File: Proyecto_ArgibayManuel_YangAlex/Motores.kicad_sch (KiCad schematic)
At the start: 10 parts, among them K1 RT314012, K2 RT314012, Q1 2N2222, Q2 2N2222, U2 DRV8871DDA, U3 DRV8871DDA

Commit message: Ordenar esquematico
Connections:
- no-connect marks 2 -> 4
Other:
- moved on the sheet: D1, D2, K1, K2, Q1, Q2, R1, R2, U2, U3

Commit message: footprint
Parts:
- R8: renamed from R2; footprint (none) -> Resistor_THT:R_Axial_DIN0204_L3.6mm_D1.6mm_P1.90mm_Vertical
- R9: renamed from R1; footprint (none) -> Resistor_THT:R_Axial_DIN0204_L3.6mm_D1.6mm_P1.90mm_Vertical
- renumbered U2 to U4, U3 to U5
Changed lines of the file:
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@@
 		(on_board yes)
 		(dnp no)
-		(property "Reference" "#PWR034"
+		(property "Reference" "#PWR017"
 			(at 153.67 96.52 0)
 			(effects
@@
 			(project "Proyecto_ArgibayManuel_YangAlex"
 				(path "/b2dde924-33f5-41ab-a1bf-811873450a89/4b87e8bb-9014-4438-949a-51563e216ea6"
-					(reference "#PWR034")
+					(reference "#PWR017")
 					(unit 1)
 				)
@@
 		(dnp no)
 		(fields_autoplaced yes)
-		(property "Reference" "R2"
+		(property "Reference" "R8"
 			(at 44.45 49.53 90)
 			(effects
@@
 			)
 		)
-		(property "Footprint" ""
+		(property "Footprint" "Resistor_THT:R_Axial_DIN0204_L3.6mm_D1.6mm_P1.90mm_Vertical"
 			(at 44.45 57.658 90)
 			(effects
@@
 			(project "Proyecto_ArgibayManuel_YangAlex"
 				(path "/b2dde924-33f5-41ab-a1bf-811873450a89/4b87e8bb-9014-4438-949a-51563e216ea6"
-					(reference "R2")
+					(reference "R8")
 					(unit 1)
 				)
@@
 		(on_board yes)
 		(dnp no)
-		(property "Reference" "#PWR036"
+		(property "Reference" "#PWR015"
 			(at 54.61 96.52 0)
 			(effects
@@
 			(project "Proyecto_ArgibayManuel_YangAlex"
 				(path "/b2dde924-33f5-41ab-a1bf-811873450a89/4b87e8bb-9014-4438-949a-51563e216ea6"
-					(reference "#PWR036")
+					(reference "#PWR015")
 					(unit 1)
 				)
@@
 		(on_board yes)
 		(dnp no)
-		(property "Reference" "#PWR033"
+		(property "Reference" "#PWR016"
 			(at 152.4 66.04 0)
 			(effects
@@
 			(project "Proyecto_ArgibayManuel_YangAlex"
 				(path "/b2dde924-33f5-41ab-a1bf-811873450a89/4b87e8bb-9014-4438-949a-51563e216ea6"
-					(reference "#PWR033")
+					(reference "#PWR016")
 					(unit 1)
 				)
@@
 		(on_board yes)
 		(dnp no)
-		(property "Reference" "#PWR035"
+		(property "Reference" "#PWR014"
 			(at 40.64 69.85 0)
 			(effects
@@
 			(project "Proyecto_ArgibayManuel_YangAlex"
 				(path "/b2dde924-33f5-41ab-a1bf-811873450a89/4b87e8bb-9014-4438-949a-51563e216ea6"
-					(reference "#PWR035")
+					(reference "#PWR014")
 					(unit 1)
 				)
@@
 		(on_board yes)
 		(dnp no)
-		(property "Reference" "U2"
+		(property "Reference" "U4"
 			(at 151.13 51.562 0)
 			(effects
@@
 			(project "Proyecto_ArgibayManuel_YangAlex"
 				(path "/b2dde924-33f5-41ab-a1bf-811873450a89/4b87e8bb-9014-4438-949a-51563e216ea6"
-					(reference "U2")
+					(reference "U4")
 					(unit 1)
 				)
@@
 		(dnp no)
 		(fields_autoplaced yes)
-		(property "Reference" "R1"
+		(property "Reference" "R9"
 			(at 58.42 77.47 90)
 			(effects
@@
 			)
 		)
-		(property "Footprint" ""
+		(property "Footprint" "Resistor_THT:R_Axial_DIN0204_L3.6mm_D1.6mm_P1.90mm_Vertical"
 			(at 58.42 85.598 90)
 			(effects
@@
 			(project "Proyecto_ArgibayManuel_YangAlex"
 				(path "/b2dde924-33f5-41ab-a1bf-811873450a89/4b87e8bb-9014-4438-949a-51563e216ea6"
-					(reference "R1")
+					(reference "R9")
 					(unit 1)
 				)
@@
 		(on_board yes)
 		(dnp no)
-		(property "Reference" "U3"
+		(property "Reference" "U5"
 			(at 152.146 82.296 0)
 			(effects
@@
 			(project "Proyecto_ArgibayManuel_YangAlex"
 				(path "/b2dde924-33f5-41ab-a1bf-811873450a89/4b87e8bb-9014-4438-949a-51563e216ea6"
-					(reference "U3")
+					(reference "U5")
 					(unit 1)
 				)

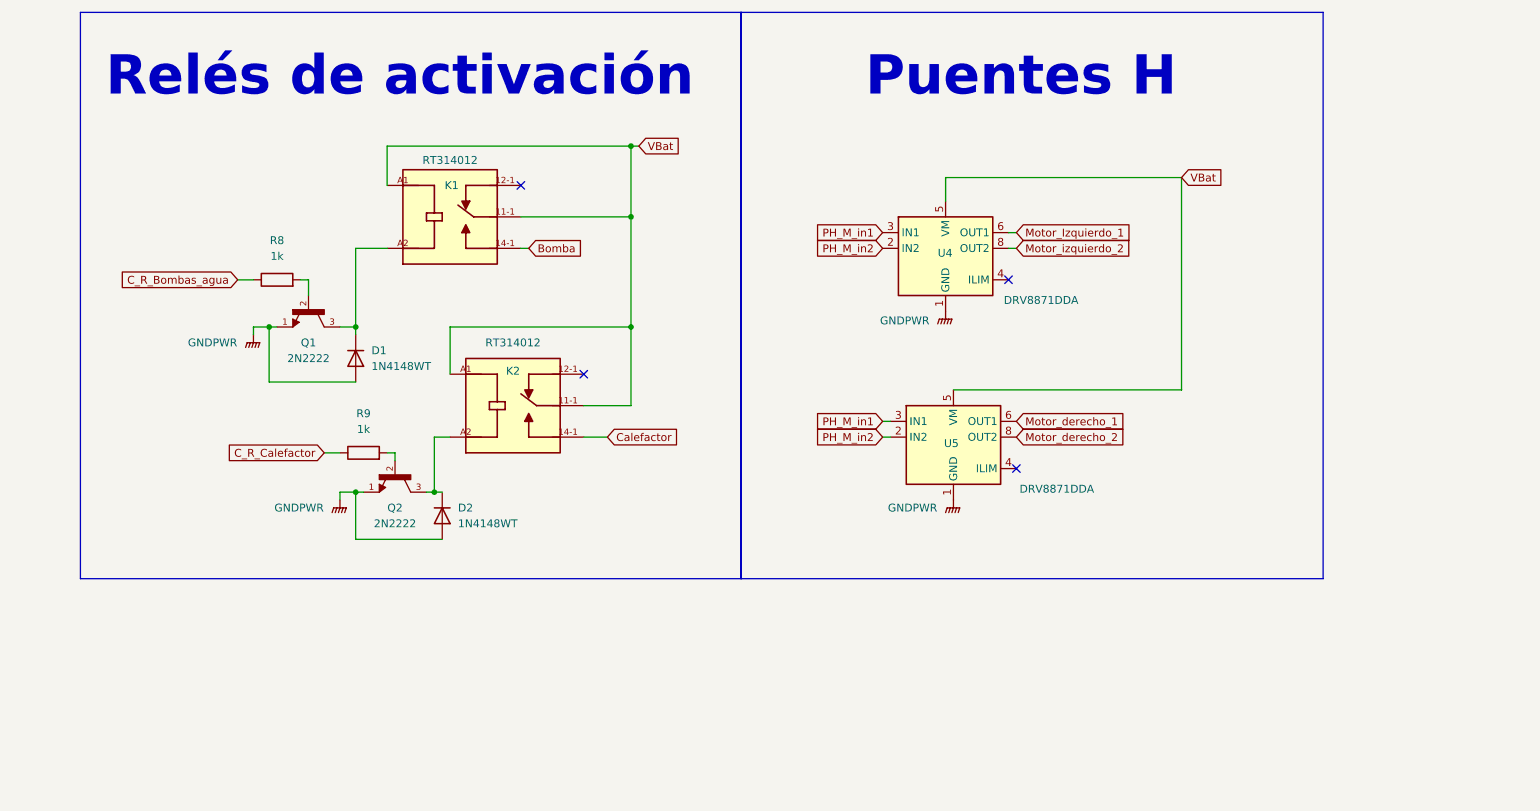
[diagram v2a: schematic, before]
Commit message: Arreglo net classes, agrego DB-9
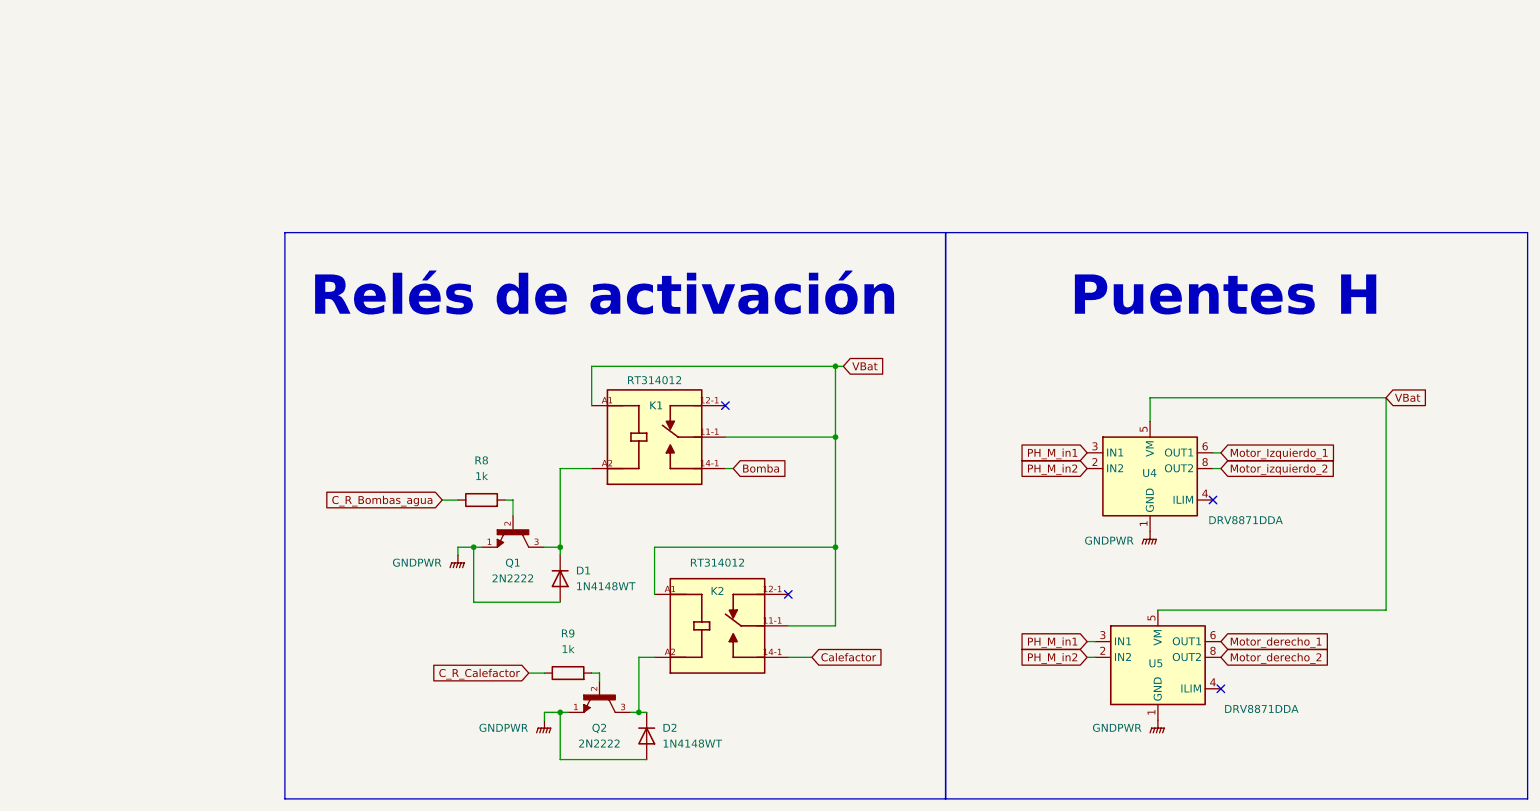
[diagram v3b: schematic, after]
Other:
- company: (none) -> Universidad de Barcelona
- title: (none) -> Circuitos de Potencia
- moved on the sheet: D1, D2, K1, K2, Q1, Q2, R8, R9, U4, U5

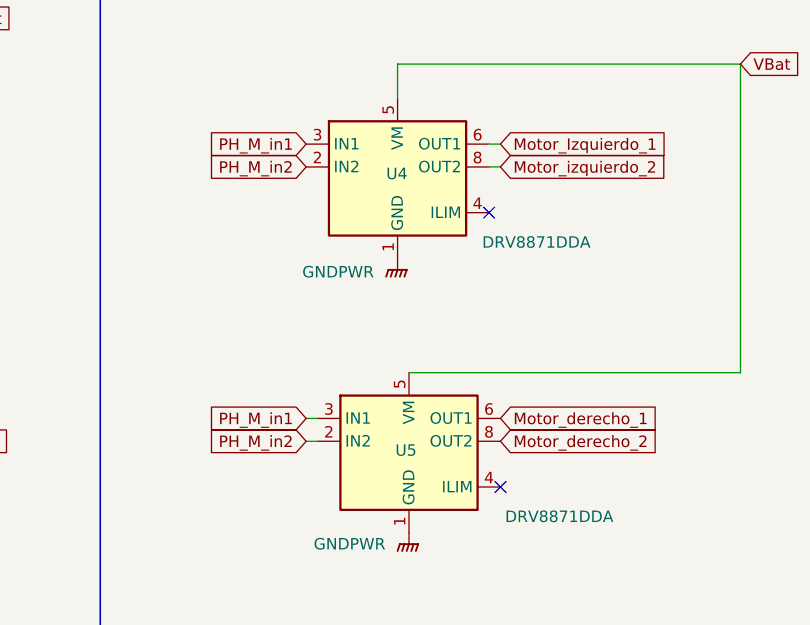
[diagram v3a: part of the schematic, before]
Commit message: Empiezo layout, cambio footprints y arreglo esquematico
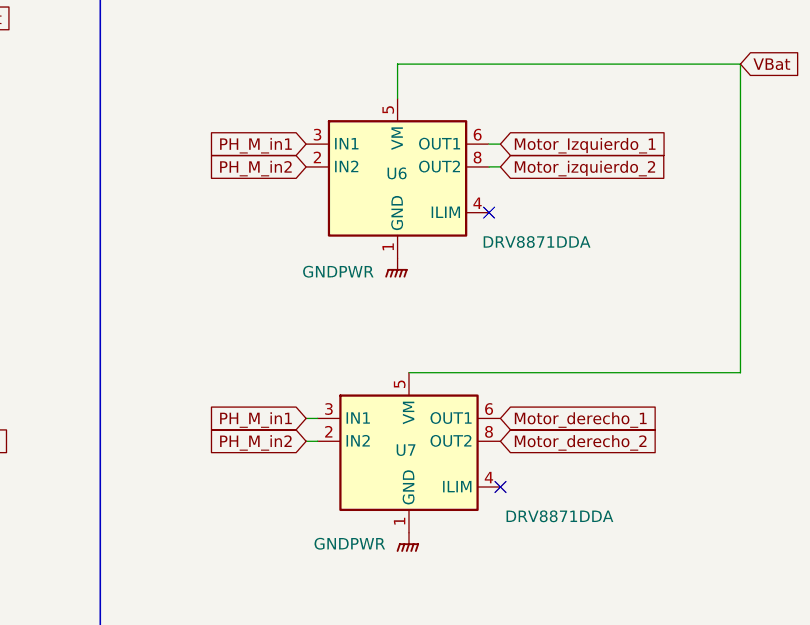
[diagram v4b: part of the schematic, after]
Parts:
- K1, K2: footprint RT314012:RELAY_9-1393239-5 -> Footprints:RT314012
- Q1, Q2: footprint 2N2222:TO127P580H530-3 -> Footprints:2N2222
- R8, R9: footprint Resistor_THT:R_Axial_DIN0204_L3.6mm_D1.6mm_P1.90mm_Vertical -> Resistor_SMD:R_0805_2012Metric
- renumbered U4 to U6, U5 to U7
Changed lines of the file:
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@@
 			)
 		)
-		(property "Footprint" "RT314012:RELAY_9-1393239-5"
+		(property "Footprint" "Footprints:RT314012"
 			(at 115.57 111.76 0)
 			(effects
@@
 		(on_board yes)
 		(dnp no)
-		(property "Reference" "#PWR017"
+		(property "Reference" "#PWR023"
 			(at 186.69 132.08 0)
 			(effects
@@
 			(project "Proyecto_ArgibayManuel_YangAlex"
 				(path "/b2dde924-33f5-41ab-a1bf-811873450a89/4b87e8bb-9014-4438-949a-51563e216ea6"
-					(reference "#PWR017")
+					(reference "#PWR023")
 					(unit 1)
 				)
@@
 			)
 		)
-		(property "Footprint" "Resistor_THT:R_Axial_DIN0204_L3.6mm_D1.6mm_P1.90mm_Vertical"
+		(property "Footprint" "Resistor_SMD:R_0805_2012Metric"
 			(at 77.47 93.218 90)
 			(effects
@@
 		(on_board yes)
 		(dnp no)
-		(property "Reference" "#PWR015"
+		(property "Reference" "#PWR021"
 			(at 87.63 132.08 0)
 			(effects
@@
 			(project "Proyecto_ArgibayManuel_YangAlex"
 				(path "/b2dde924-33f5-41ab-a1bf-811873450a89/4b87e8bb-9014-4438-949a-51563e216ea6"
-					(reference "#PWR015")
+					(reference "#PWR021")
 					(unit 1)
 				)
@@
 		(on_board yes)
 		(dnp no)
-		(property "Reference" "#PWR016"
+		(property "Reference" "#PWR022"
 			(at 185.42 101.6 0)
 			(effects
@@
 			(project "Proyecto_ArgibayManuel_YangAlex"
 				(path "/b2dde924-33f5-41ab-a1bf-811873450a89/4b87e8bb-9014-4438-949a-51563e216ea6"
-					(reference "#PWR016")
+					(reference "#PWR022")
 					(unit 1)
 				)
@@
 			)
 		)
-		(property "Footprint" "RT314012:RELAY_9-1393239-5"
+		(property "Footprint" "Footprints:RT314012"
 			(at 105.41 81.28 0)
 			(effects
@@
 			)
 		)
-		(property "Footprint" "2N2222:TO127P580H530-3"
+		(property "Footprint" "Footprints:2N2222"
 			(at 96.52 123.19 0)
 			(effects
@@
 			)
 		)
-		(property "Footprint" "2N2222:TO127P580H530-3"
+		(property "Footprint" "Footprints:2N2222"
 			(at 82.55 96.52 0)
 			(effects
@@
 		(on_board yes)
 		(dnp no)
-		(property "Reference" "#PWR014"
+		(property "Reference" "#PWR020"
 			(at 73.66 105.41 0)
 			(effects
@@
 			(project "Proyecto_ArgibayManuel_YangAlex"
 				(path "/b2dde924-33f5-41ab-a1bf-811873450a89/4b87e8bb-9014-4438-949a-51563e216ea6"
-					(reference "#PWR014")
+					(reference "#PWR020")
 					(unit 1)
 				)
@@
 		(on_board yes)
 		(dnp no)
-		(property "Reference" "U4"
+		(property "Reference" "U6"
 			(at 184.15 87.122 0)
 			(effects
@@
 			(project "Proyecto_ArgibayManuel_YangAlex"
 				(path "/b2dde924-33f5-41ab-a1bf-811873450a89/4b87e8bb-9014-4438-949a-51563e216ea6"
-					(reference "U4")
+					(reference "U6")
 					(unit 1)
 				)
@@
 			)
 		)
-		(property "Footprint" "Resistor_THT:R_Axial_DIN0204_L3.6mm_D1.6mm_P1.90mm_Vertical"
+		(property "Footprint" "Resistor_SMD:R_0805_2012Metric"
 			(at 91.44 121.158 90)
 			(effects
@@
 		(on_board yes)
 		(dnp no)
-		(property "Reference" "U5"
+		(property "Reference" "U7"
 			(at 185.166 117.856 0)
 			(effects
@@
 			(project "Proyecto_ArgibayManuel_YangAlex"
 				(path "/b2dde924-33f5-41ab-a1bf-811873450a89/4b87e8bb-9014-4438-949a-51563e216ea6"
-					(reference "U5")
+					(reference "U7")
 					(unit 1)
 				)

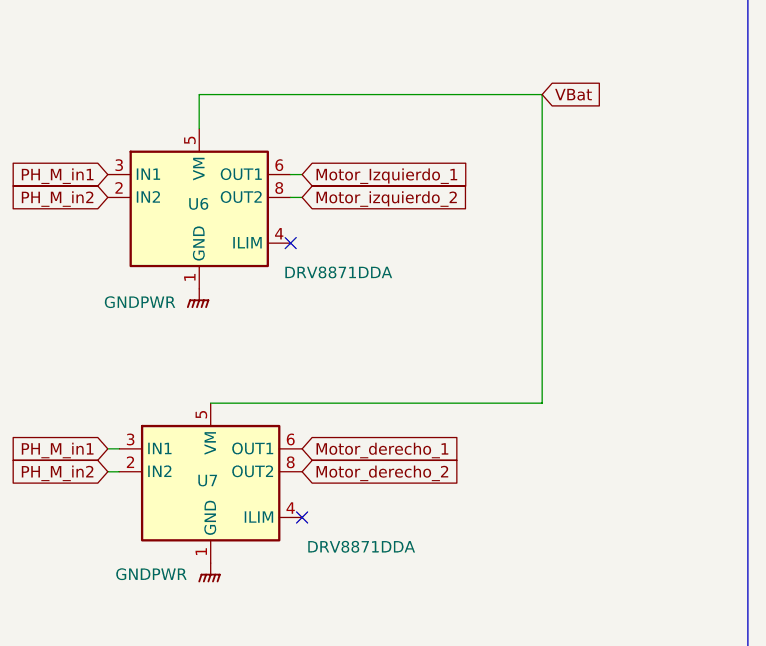
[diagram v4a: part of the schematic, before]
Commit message: Cambio layout (faltan agregar vías y reorganizar con la capa BOTTOM)
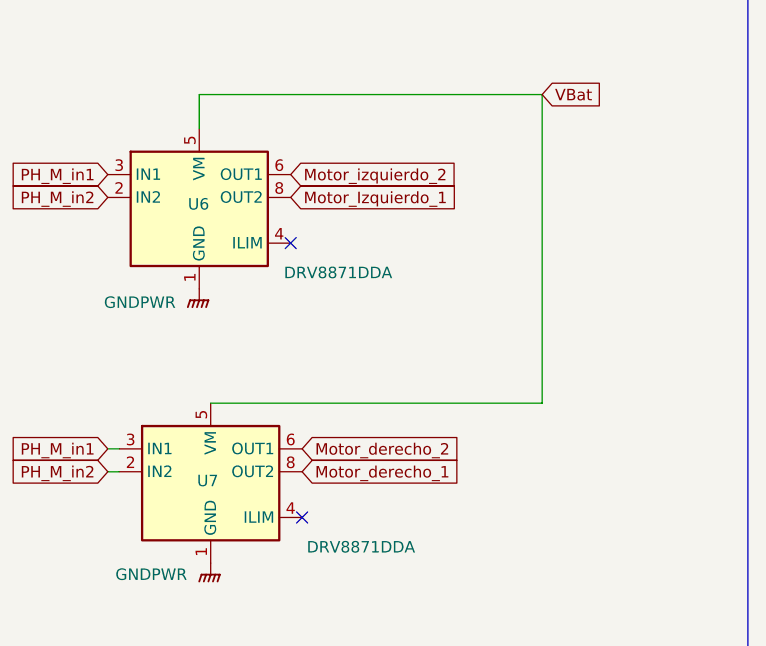
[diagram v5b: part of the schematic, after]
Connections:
- net Motor_Izquierdo_1: now also U6.8 (OUT2); no longer U6.6 (OUT1)
- net Motor_derecho_1: now also U7.8 (OUT2); no longer U7.6 (OUT1)
- net Motor_derecho_2: now also U7.6 (OUT1); no longer U7.8 (OUT2)
- net Motor_izquierdo_2: now also U6.6 (OUT1); no longer U6.8 (OUT2)

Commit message: Arreglo layout y esqumatico con las correcciones pasadas
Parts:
- added R14, R15: 1k, Resistor_SMD:R_0805_2012Metric, symbol Device:R
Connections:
- net C_R_Bombas_agua: now also R8.2; no longer R8.1
- net C_R_Calefactor: now also R9.2; no longer R9.1
- net GNDPWR: now also R14.2, R15.2; no longer D1.2 (A), D2.2 (A)
- net VBat: now also D1.1 (K), D2.1 (K)
- net at K2.A2, Q2.3: now also D2.2 (A), R15.1; no longer D2.1 (K)
- net at Q1.2: now also R8.1; no longer R8.2
- net at K1.A2, Q1.3: now also D1.2 (A), R14.1; no longer D1.1 (K)
- net at Q2.2: now also R9.1; no longer R9.2
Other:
- moved on the sheet: D1, D2, Q1, Q2, R8, R9

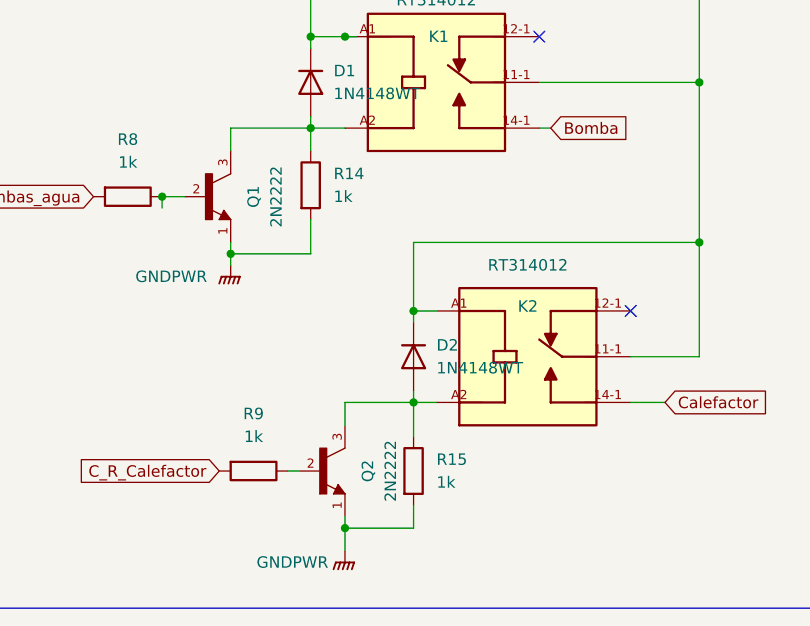
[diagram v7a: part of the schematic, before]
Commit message: Separacion de Botonera
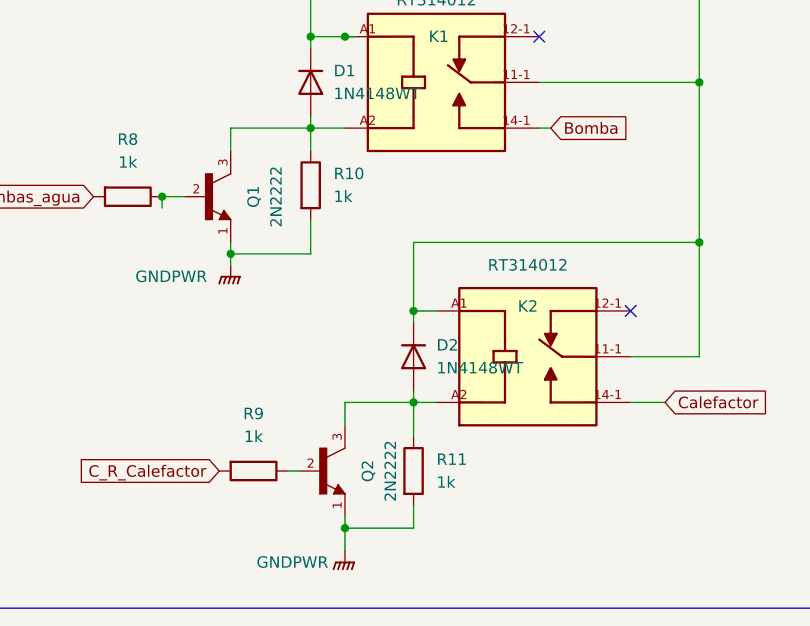
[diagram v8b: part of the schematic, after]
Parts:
- renumbered R14 to R10, R15 to R11
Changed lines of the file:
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@@
 		(on_board yes)
 		(dnp no)
-		(property "Reference" "#PWR024"
+		(property "Reference" "#PWR027"
 			(at 186.69 132.08 0)
 			(effects
@@
 			(project "Proyecto_ArgibayManuel_YangAlex"
 				(path "/b2dde924-33f5-41ab-a1bf-811873450a89/4b87e8bb-9014-4438-949a-51563e216ea6"
-					(reference "#PWR024")
+					(reference "#PWR027")
 					(unit 1)
 				)
@@
 		(on_board yes)
 		(dnp no)
-		(property "Reference" "#PWR022"
+		(property "Reference" "#PWR025"
 			(at 95.25 138.43 0)
 			(effects
@@
 			(project "Proyecto_ArgibayManuel_YangAlex"
 				(path "/b2dde924-33f5-41ab-a1bf-811873450a89/4b87e8bb-9014-4438-949a-51563e216ea6"
-					(reference "#PWR022")
+					(reference "#PWR025")
 					(unit 1)
 				)
@@
 		(on_board yes)
 		(dnp no)
-		(property "Reference" "#PWR023"
+		(property "Reference" "#PWR026"
 			(at 185.42 101.6 0)
 			(effects
@@
 			(project "Proyecto_ArgibayManuel_YangAlex"
 				(path "/b2dde924-33f5-41ab-a1bf-811873450a89/4b87e8bb-9014-4438-949a-51563e216ea6"
-					(reference "#PWR023")
+					(reference "#PWR026")
 					(unit 1)
 				)
@@
 		(dnp no)
 		(fields_autoplaced yes)
-		(property "Reference" "R15"
+		(property "Reference" "R11"
 			(at 105.41 123.1899 0)
 			(effects
@@
 			(project "Proyecto_ArgibayManuel_YangAlex"
 				(path "/b2dde924-33f5-41ab-a1bf-811873450a89/4b87e8bb-9014-4438-949a-51563e216ea6"
-					(reference "R15")
+					(reference "R11")
 					(unit 1)
 				)
@@
 		(on_board yes)
 		(dnp no)
-		(property "Reference" "#PWR021"
+		(property "Reference" "#PWR024"
 			(at 82.55 106.68 0)
 			(effects
@@
 			(project "Proyecto_ArgibayManuel_YangAlex"
 				(path "/b2dde924-33f5-41ab-a1bf-811873450a89/4b87e8bb-9014-4438-949a-51563e216ea6"
-					(reference "#PWR021")
+					(reference "#PWR024")
 					(unit 1)
 				)
@@
 		(dnp no)
 		(fields_autoplaced yes)
-		(property "Reference" "R14"
+		(property "Reference" "R10"
 			(at 93.98 91.4399 0)
 			(effects
@@
 			(project "Proyecto_ArgibayManuel_YangAlex"
 				(path "/b2dde924-33f5-41ab-a1bf-811873450a89/4b87e8bb-9014-4438-949a-51563e216ea6"
-					(reference "R14")
+					(reference "R10")
 					(unit 1)
 				)
